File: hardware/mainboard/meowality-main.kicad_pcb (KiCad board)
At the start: 6 copper layers, 200 x 75 mm, 266 parts, among them J1 Micro_SD_Card_Det, J2 MINI_DP_SINK, J3 DEBUG, J4 USB_C_Receptacle, J5 Conn_01x02, J6 Conn_01x02, P1 M2_SOCKET_E, Q1 BSS138, Q10 BSS138, Q2 BSS138, Q3 BSS138, Q5 BSS138, Q7 BSS138, SW1 SW_DIP_x04, SW2 SW_Push, SW3 SW_Push, SW4 SW_Push, SW5 SW_Push, SW6 SW_Push, U1 CP3225-100.000-3.3-25-X-T-TR, U10 MMC5983MA, U11 Si52112-B, U12 TPD4E02B04DQA, U13 TPD4E02B04DQA, U14 CBTL02043A, U15 FUSB302B11MPX, U16 USB3318, U17 AP6230xWU, U19 ADP5070ACPZ, U2 AX3HAF1-135.0000T, U20 CAT4106HV4, U21 74LVC2T45DC, U3 AP6230xWU, U4 AP6230xWU, U5 SiC438, U6 AP6230xWU, U7 AP6230xWU, U8 TXS02612, U9 ICM-20789, X1 831056169, Y1 25MHz

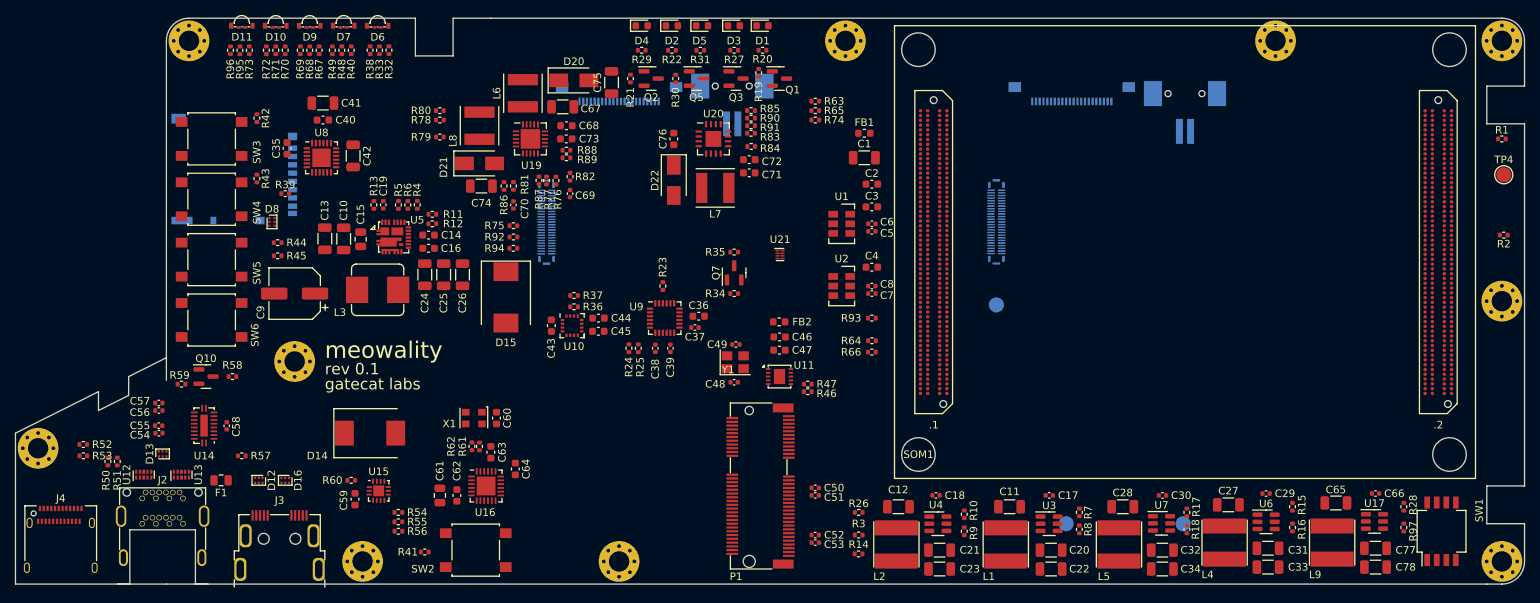
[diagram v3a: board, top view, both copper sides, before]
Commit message: Begin some routing
Signed-off-by: gatecat <gatecat@ds0.me>
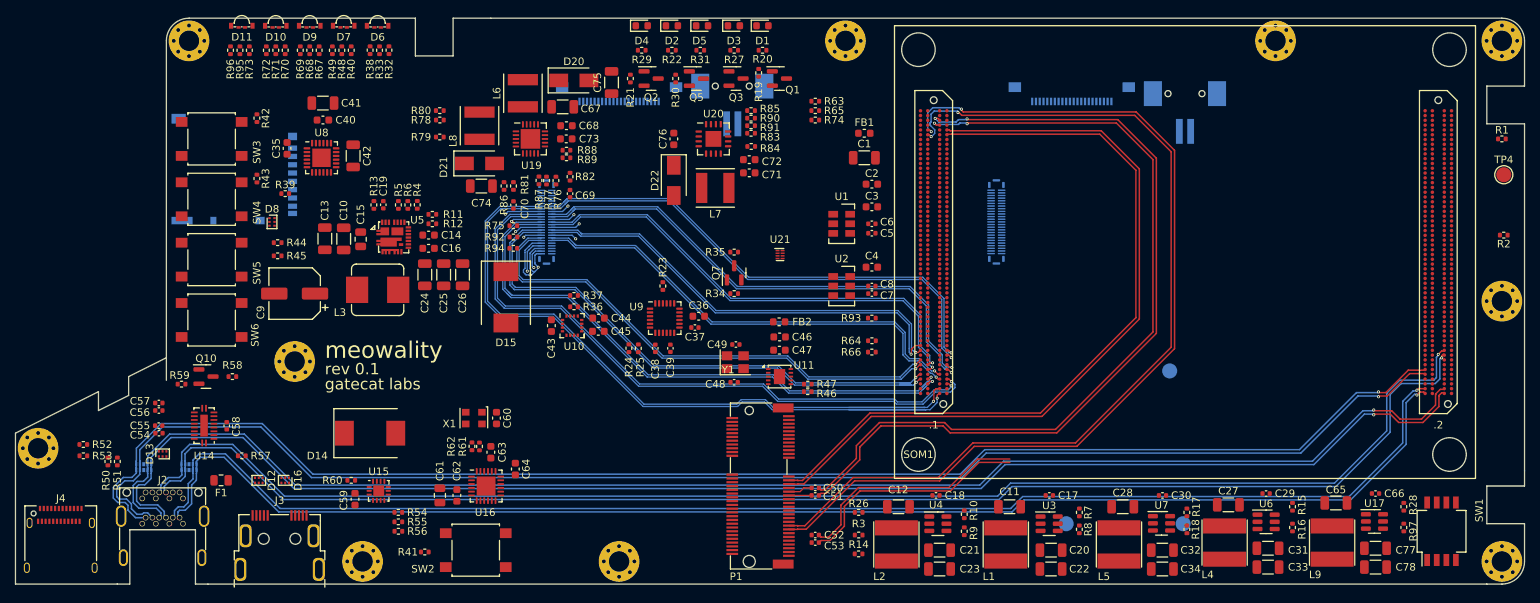
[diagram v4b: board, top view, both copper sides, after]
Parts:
- U12, U13: moved to B.Cu
- moved TP1 24.6 mm to (183.0, 106.8)
- moved U13 1.41 mm to (53.0, 119.5), turned to -90 degrees
- moved U12 1.00 mm to (47.0, 119.5), turned to -90 degrees
- moved C5 0.25 mm to (143.5, 88.5)
- turned C50 to 180 degrees
- turned C51 to 180 degrees
- turned C53 to 180 degrees
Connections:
- SOM1 pad 1A10: unconnected-(SOM1-Pad1A10) -> DSI0B_D0-
- SOM1 pad 1A3: DSI0B_D0+ -> DSI0B_CLK+
- SOM1 pad 1A4: DSI0B_D0- -> DSI0B_CLK-
- SOM1 pad 1A6: unconnected-(SOM1-Pad1A6) -> DSI0B_D1+
- SOM1 pad 1A7: unconnected-(SOM1-Pad1A7) -> DSI0B_D1-
- SOM1 pad 1A9: unconnected-(SOM1-Pad1A9) -> DSI0B_D0+
- SOM1 pad 1B1: DSI0B_CLK+ -> DSI0B_D3-
- SOM1 pad 1B2: DSI0B_CLK- -> DSI0B_D3+
- SOM1 pad 1B4: DSI0A_D3+ -> DSI0A_D3-
- SOM1 pad 1B5: DSI0A_D3- -> DSI0A_D3+
- SOM1 pad 1B7: DSI0B_D1+ -> unconnected-(SOM1-Pad1B7)
- SOM1 pad 1B8: DSI0B_D1- -> unconnected-(SOM1-Pad1B8)
- SOM1 pad 1C10: DSI0B_D2- -> unconnected-(SOM1-Pad1C10)
- SOM1 pad 1C3: DSI0A_CLK+ -> DSI0B_D2-
- SOM1 pad 1C4: DSI0A_CLK- -> DSI0B_D2+
- SOM1 pad 1C6: DSI0A_D2+ -> DSI0A_D2-
- SOM1 pad 1C7: DSI0A_D2- -> DSI0A_D2+
- SOM1 pad 1C9: DSI0B_D2+ -> unconnected-(SOM1-Pad1C9)
- SOM1 pad 1D10: DSI0B_D3+ -> DSI0A_CLK+
- SOM1 pad 1D11: DSI0B_D3- -> DSI0A_CLK-
- U12 pad 10: unconnected-(U12-Pad10) -> DP_IN_L3-
- U12 pad 6: unconnected-(U12-Pad6) -> DP_IN_L2+
- U12 pad 7: unconnected-(U12-Pad7) -> DP_IN_L2-
- U12 pad 9: unconnected-(U12-Pad9) -> DP_IN_L3+
- U13 pad 10: unconnected-(U13-Pad10) -> DP_IN_L0-
- U13 pad 6: unconnected-(U13-Pad6) -> DP_IN_L1+
- U13 pad 7: unconnected-(U13-Pad7) -> DP_IN_L1-
- U13 pad 9: unconnected-(U13-Pad9) -> DP_IN_L0+
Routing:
- net DP_IN_L2-: track 0.00 -> 195.4 mm, vias 0 -> 1
- net DP_IN_L3-: track 0.00 -> 195.3 mm, vias 0 -> 1
- net DP_IN_L3+: track 0.00 -> 194.8 mm, vias 0 -> 1
- net DP_IN_L2+: track 0.00 -> 194.7 mm, vias 0 -> 1
- net DP_IN_L0-: track 0.00 -> 190.7 mm, vias 0 -> 1
- net DP_IN_L0+: track 0.00 -> 190.0 mm, vias 0 -> 1
- net DP_IN_L1-: track 0.00 -> 185.7 mm, vias 0 -> 1
- net DP_IN_L1+: track 0.00 -> 185.1 mm, vias 0 -> 1
- net PCIE_C2M_L1-: track 0.00 -> 126.0 mm, vias 0 -> 2
- net PCIE_C2M_L1+: track 0.00 -> 124.8 mm, vias 0 -> 2
- net PCIE_M2C_L0-: track 0.00 -> 111.1 mm, vias 0 -> 2
- net PCIE_M2C_L0+: track 0.00 -> 109.6 mm, vias 0 -> 2
- net PCIE_C2M_L0-: track 0.00 -> 103.0 mm
- net PCIE_C2M_L0+: track 0.00 -> 101.5 mm
- net DSI0B_D3-: track 0.00 -> 97.6 mm, vias 0 -> 1
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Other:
- outline, holes or cut-outs redrawn

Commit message: First pass high-speed routing
Signed-off-by: gatecat <gatecat@ds0.me>
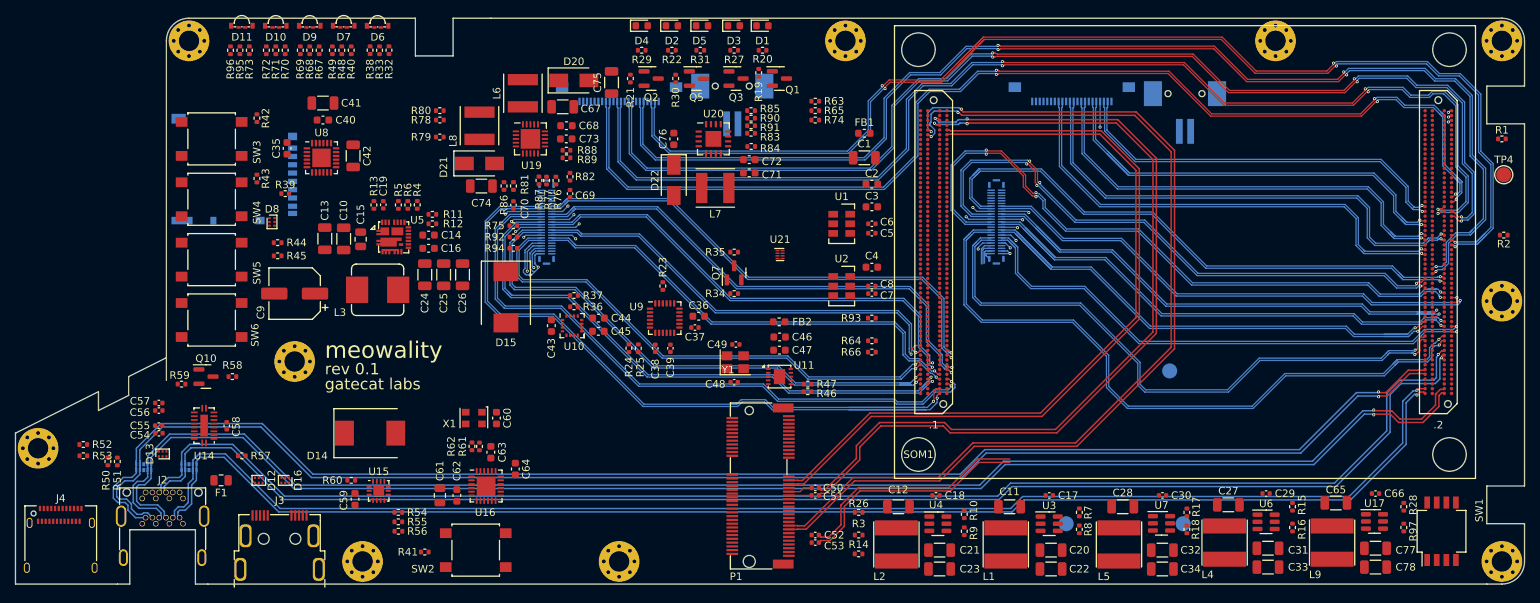
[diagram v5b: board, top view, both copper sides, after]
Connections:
- SOM1 pad 2A14: DSI1B_D2+ -> DSI1A_D3-
- SOM1 pad 2A15: DSI1B_D2- -> DSI1A_D3+
- SOM1 pad 2A32: CSI1_D3+ -> CSI1_D0-
- SOM1 pad 2A33: CSI1_D3- -> CSI1_D0+
- SOM1 pad 2A38: CSI1_CLK+ -> CSI1_CLK-
- SOM1 pad 2A39: CSI1_CLK- -> CSI1_CLK+
- SOM1 pad 2A41: CSI0_D2+ -> CSI1_D3-
- SOM1 pad 2A42: CSI0_D2- -> CSI1_D3+
- SOM1 pad 2B12: unconnected-(SOM1-Pad2B12) -> DSI1A_D1+
- SOM1 pad 2B13: unconnected-(SOM1-Pad2B13) -> DSI1A_D1-
- SOM1 pad 2B15: DSI1B_D1+ -> DSI1A_D2-
- SOM1 pad 2B16: DSI1B_D1- -> DSI1A_D2+
- SOM1 pad 2B18: DSI1B_CLK+ -> unconnected-(SOM1-Pad2B18)
- SOM1 pad 2B19: DSI1B_CLK- -> unconnected-(SOM1-Pad2B19)
- SOM1 pad 2B21: unconnected-(SOM1-Pad2B21) -> DSI1B_D2-
- SOM1 pad 2B22: unconnected-(SOM1-Pad2B22) -> DSI1B_D2+
- SOM1 pad 2B24: DSI1A_D2+ -> DSI1B_D3-
- SOM1 pad 2B25: DSI1A_D2- -> DSI1B_D3+
- SOM1 pad 2B33: CSI1_D0+ -> CSI0_D2+
- SOM1 pad 2B34: CSI1_D0- -> CSI0_D2-
- SOM1 pad 2B39: CSI1_D2+ -> CSI1_D2-
- SOM1 pad 2B40: CSI1_D2- -> CSI1_D2+
- SOM1 pad 2C11: DSI1B_D3+ -> unconnected-(SOM1-Pad2C11)
- SOM1 pad 2C12: DSI1B_D3- -> unconnected-(SOM1-Pad2C12)
- SOM1 pad 2C17: DSI1A_D1+ -> DSI1B_D1+
- SOM1 pad 2C18: DSI1A_D1- -> DSI1B_D1-
- SOM1 pad 2C26: CSI1_D1+ -> CSI1_D1-
- SOM1 pad 2C27: CSI1_D1- -> CSI1_D1+
- SOM1 pad 2D15: DSI1A_CLK+ -> DSI1A_CLK-
- SOM1 pad 2D16: DSI1A_CLK- -> DSI1A_CLK+
- SOM1 pad 2D21: DSI1A_D3+ -> unconnected-(SOM1-Pad2D21)
- SOM1 pad 2D22: DSI1A_D3- -> unconnected-(SOM1-Pad2D22)
- SOM1 pad 2D24: unconnected-(SOM1-Pad2D24) -> DSI1B_CLK-
- SOM1 pad 2D25: unconnected-(SOM1-Pad2D25) -> DSI1B_CLK+
- SOM1 pad 2D30: CSI0_D0+ -> CSI0_D3+
- SOM1 pad 2D31: CSI0_D0- -> CSI0_D3-
- SOM1 pad 2D39: CSI0_D3+ -> CSI0_D0+
- SOM1 pad 2D40: CSI0_D3- -> CSI0_D0-
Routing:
- net CSI1_D0-: track 0.00 -> 159.7 mm, vias 0 -> 3
- net CSI1_D1-: track 0.00 -> 159.1 mm, vias 0 -> 3
- net CSI1_D0+: track 0.00 -> 158.9 mm, vias 0 -> 3
- net CSI1_D1+: track 0.00 -> 158.2 mm, vias 0 -> 3
- net CSI1_D2-: track 0.00 -> 153.7 mm, vias 0 -> 3
- net CSI1_D2+: track 0.00 -> 153.3 mm, vias 0 -> 3
- net CSI1_CLK-: track 0.00 -> 151.0 mm, vias 0 -> 3
- net CSI1_D3-: track 0.00 -> 150.7 mm, vias 0 -> 3
- net CSI1_CLK+: track 0.00 -> 150.5 mm, vias 0 -> 3
- net CSI1_D3+: track 0.00 -> 149.7 mm, vias 0 -> 3
- net DSI1A_D1+: track 0.00 -> 90.9 mm, vias 0 -> 1
- net DSI1A_D1-: track 0.00 -> 90.0 mm, vias 0 -> 1
- net DSI1B_D2+: track 0.00 -> 89.4 mm, vias 0 -> 3
- net DSI1B_D2-: track 0.00 -> 88.4 mm, vias 0 -> 3
- net DSI1A_D0+: track 0.00 -> 81.5 mm, vias 0 -> 1
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
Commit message: High speed bits routed
Signed-off-by: gatecat <gatecat@ds0.me>
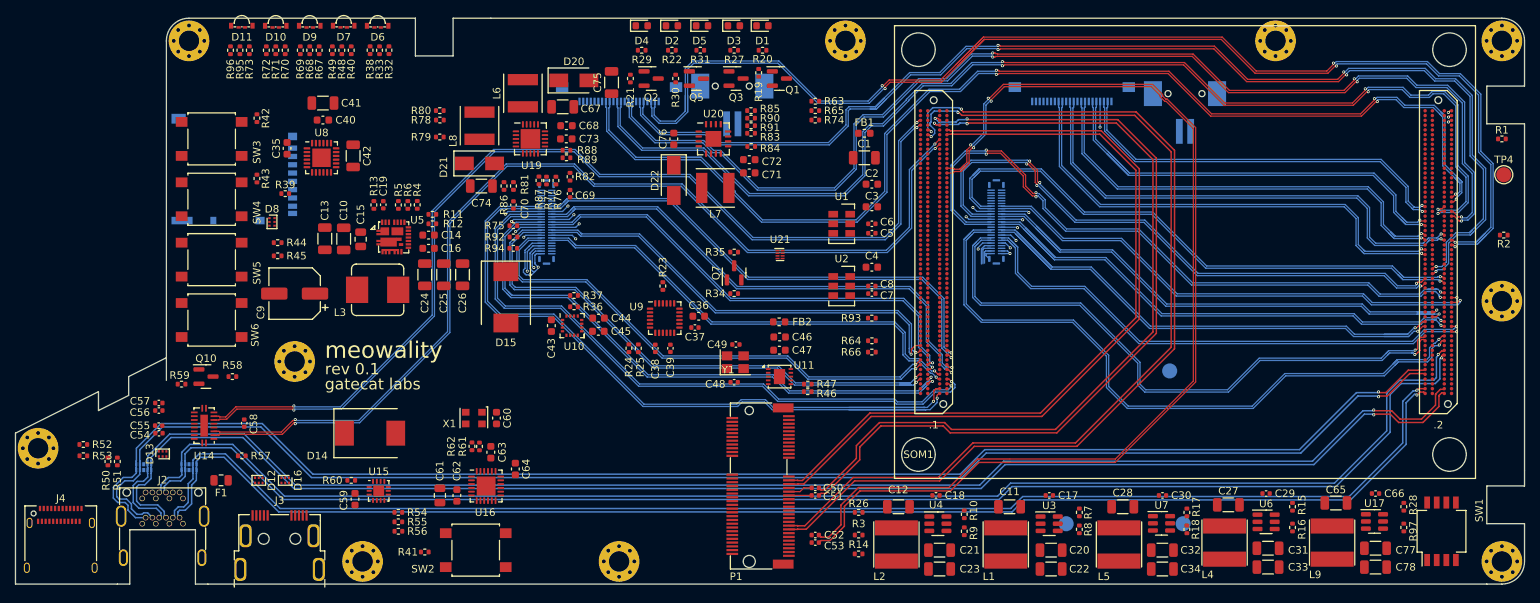
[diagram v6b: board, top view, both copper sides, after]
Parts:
- moved C58 2.35 mm to (60.3, 113.7)
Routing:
- net GTR_LEFT_C2M-: track 0.00 -> 134.8 mm, vias 0 -> 2
- net GTR_LEFT_C2M+: track 0.00 -> 134.7 mm, vias 0 -> 2
- net GTR_LEFT_M2C-: track 0.00 -> 134.2 mm, vias 0 -> 2
- net GTR_LEFT_M2C+: track 0.00 -> 134.1 mm, vias 0 -> 2
- net PCIE_M2C_L1-: track 31.2 -> 138.4 mm, vias 0 -> 2
- net PCIE_M2C_L1+: track 31.2 -> 137.5 mm, vias 0 -> 2
- net CSI1_D3-: track 150.7 -> 154.7 mm
- net CSI1_D3+: track 149.7 -> 153.7 mm
- net CSI1_D1-: track 159.1 -> 155.5 mm
- net CSI1_D1+: track 158.2 -> 155.0 mm
- net CSI1_D0+: track 158.9 -> 161.7 mm
- net CSI1_D0-: track 159.7 -> 162.4 mm
- net CSI1_D2-: track 153.7 -> 152.3 mm
- net CSI1_D2+: track 153.3 -> 151.9 mm

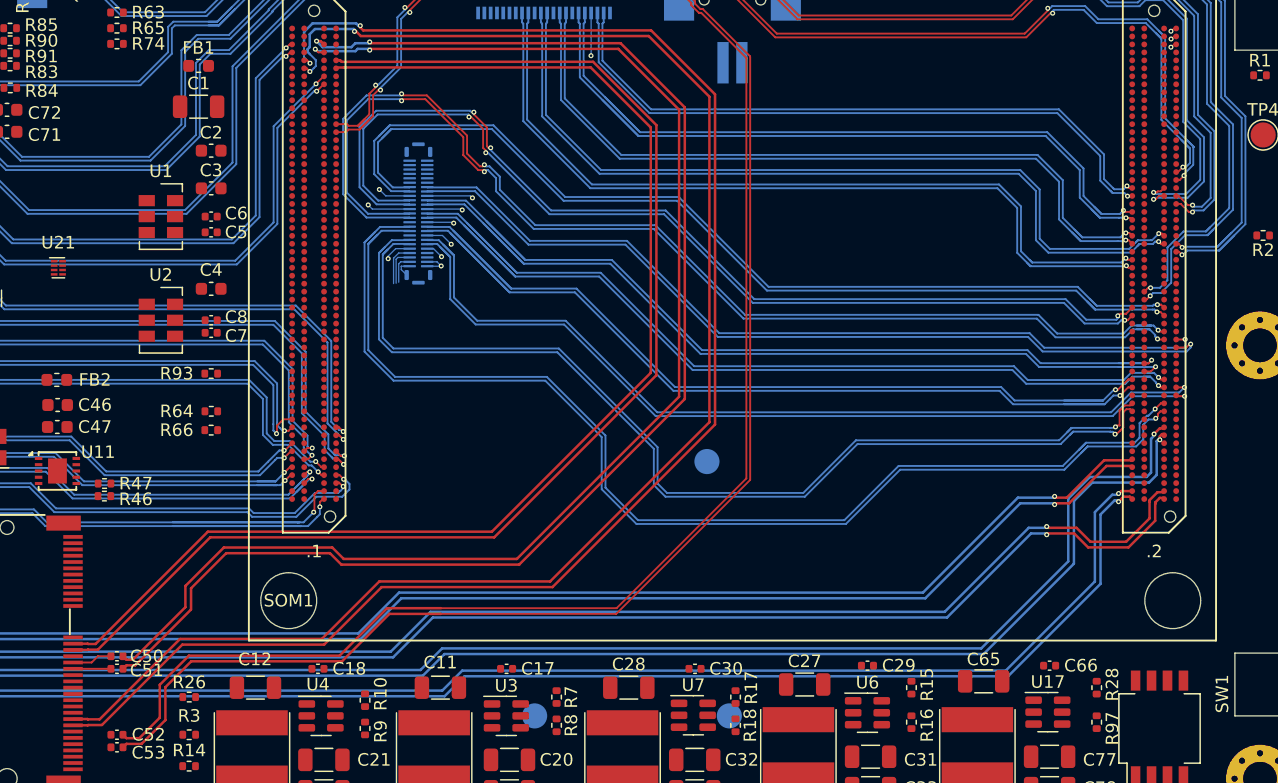
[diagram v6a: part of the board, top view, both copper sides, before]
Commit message: Misc signal breakout/routing
Signed-off-by: gatecat <gatecat@ds0.me>
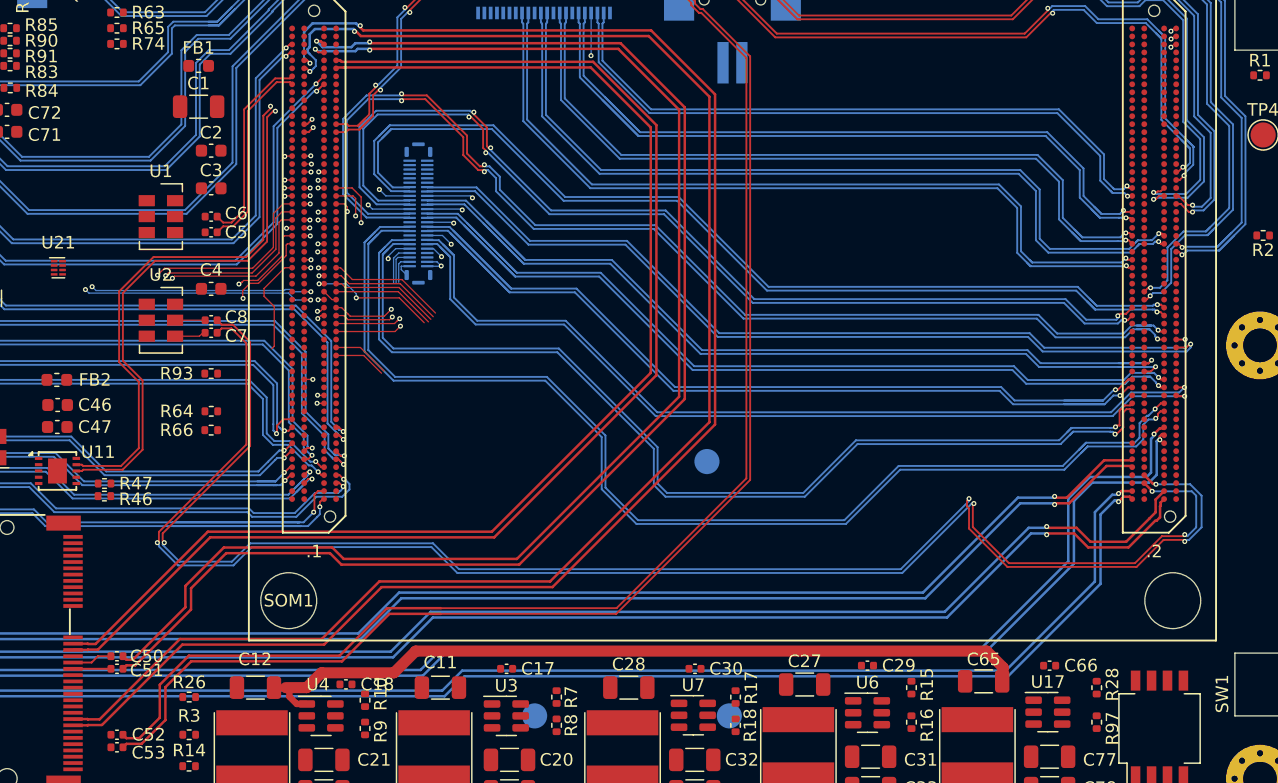
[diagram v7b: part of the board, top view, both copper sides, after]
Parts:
- moved C18 2.55 mm to (154.2, 124.5)
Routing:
- net /SOM/REFCLK135-: track 0.00 -> 122.6 mm, vias 0 -> 4
- net /SOM/REFCLK135+: track 0.00 -> 120.6 mm, vias 0 -> 4
- net SD_D2_1V8: track 0.00 -> 103.9 mm, vias 0 -> 1
- net SD_D1_1V8: track 0.00 -> 102.1 mm, vias 0 -> 1
- net SD_~{CD}_1V8: track 0.00 -> 99.8 mm, vias 0 -> 1
- net SD_D0_1V8: track 0.00 -> 99.3 mm, vias 0 -> 1
- net +5V: track 0.00 -> 63.4 mm
- net PCIE_REFCLK+: track 0.00 -> 48.0 mm, vias 0 -> 2
- net PCIE_REFCLK-: track 0.00 -> 47.6 mm, vias 0 -> 2
- net SPI_C2M: track 0.00 -> 46.9 mm, vias 0 -> 1
- net SPI_SCLK: track 0.00 -> 46.5 mm, vias 0 -> 1
- net SPI_M2C: track 0.00 -> 45.9 mm, vias 0 -> 1
- net SPI_~{CS}: track 0.00 -> 43.7 mm, vias 0 -> 1
- net JTAG_TCK: track 0.00 -> 38.1 mm, vias 0 -> 1
- net JTAG_TDI: track 0.00 -> 36.6 mm, vias 0 -> 1
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
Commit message: Finish SD/ULPI routes
Signed-off-by: gatecat <gatecat@ds0.me>
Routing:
- net ULPI_NXT: track 0.70 -> 127.3 mm, vias 1 -> 4
- net ULPI_~{RST}: track 0.59 -> 126.3 mm, vias 1 -> 2
- net ULPI_STP: track 0.48 -> 125.4 mm, vias 1 -> 2
- net ULPI_D1: track 0.66 -> 124.7 mm, vias 1 -> 2
- net ULPI_D3: track 0.58 -> 123.2 mm, vias 1 -> 4
- net ULPI_D0: track 0.68 -> 122.2 mm, vias 1 -> 2
- net ULPI_D4: track 0.54 -> 118.8 mm, vias 1 -> 2
- net SD_D3_1V8: track 3.14 -> 113.6 mm, vias 1 -> 2
- net SD_CMD_1V8: track 3.01 -> 110.1 mm, vias 1 -> 2
- net SD_CLK_1V8: track 2.45 -> 107.6 mm, vias 1 -> 2
- net ULPI_D7: track 25.6 -> 114.0 mm, vias 1 -> 2
- net ULPI_D6: track 24.1 -> 111.5 mm, vias 1 -> 2
- net ULPI_D5: track 22.4 -> 108.2 mm, vias 1 -> 2
- net ULPI_CLK: track 12.9 -> 77.9 mm, vias 1 -> 2
- net ULPI_D2: track 14.6 -> 76.3 mm, vias 1 -> 2
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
